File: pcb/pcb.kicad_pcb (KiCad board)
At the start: 2 copper layers, 30 parts, among them J1 USB_C_Receptacle_PowerOnly_6P, J10 Screw_Terminal_01x03, J2 Conn_01x04_Pin, J3 Screw_Terminal_01x03, J4 Screw_Terminal_01x04, J5 Screw_Terminal_01x02, J6 Screw_Terminal_01x02, J7 Screw_Terminal_01x04, J8 Screw_Terminal_01x07, J9 Screw_Terminal_01x02, K1 SANYOU_SRD_Form_A, Q1 2N2222A, Q2 AO3400A, U1 AMS1117-3.3, U2 ESP32-C6-MINI-1, U3 AM2302

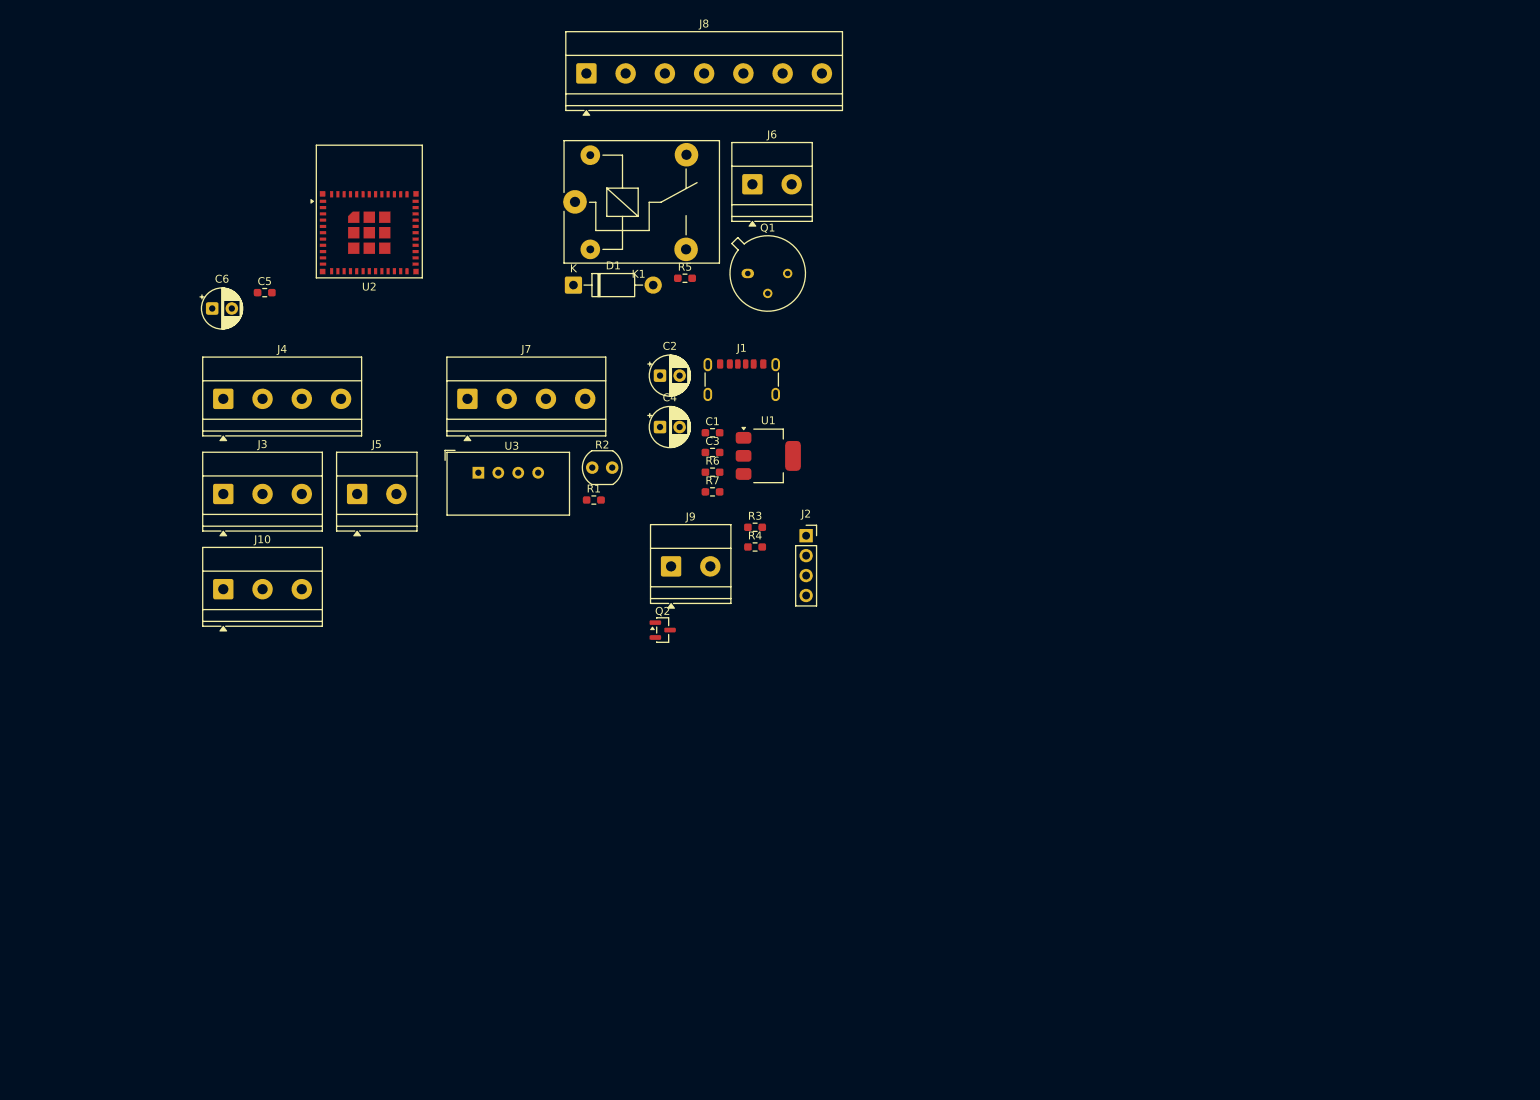
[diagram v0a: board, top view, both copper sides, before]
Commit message: placing the components
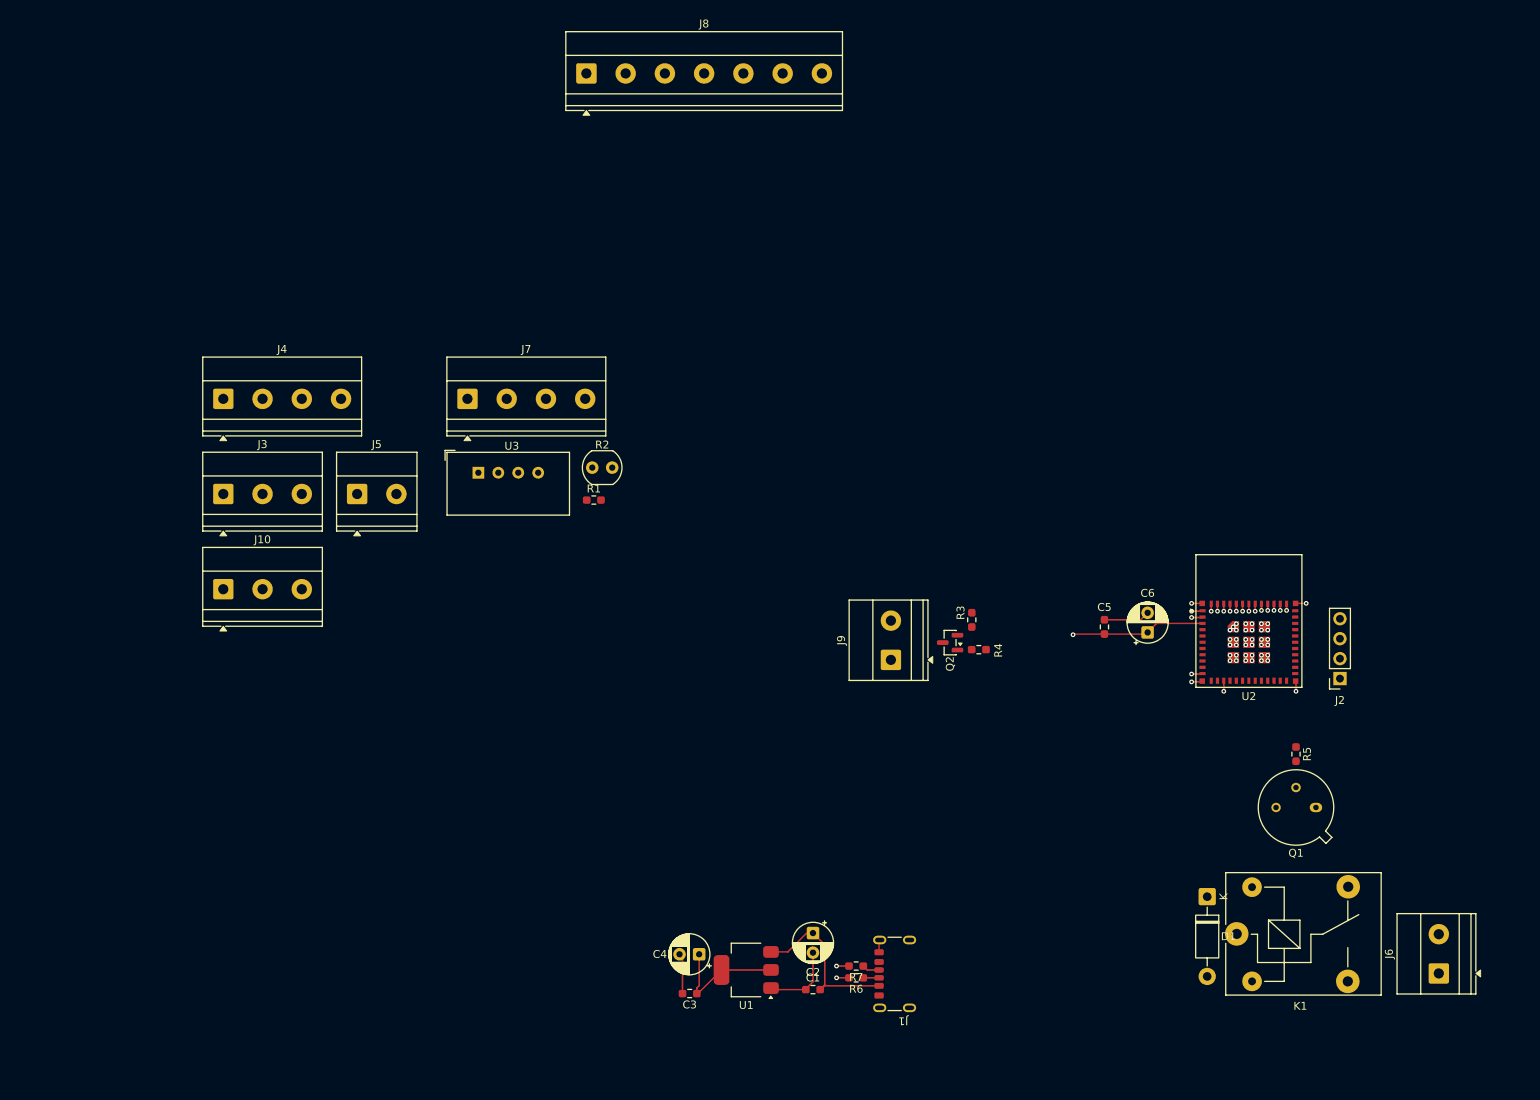
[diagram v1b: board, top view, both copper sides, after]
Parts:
- moved J6 133.2 mm to (244.1, 140.1), turned to 90 degrees
- moved C6 126.1 mm to (207.0, 96.7), turned to 90 degrees
- moved K1 125.7 mm to (218.3, 135.1)
- moved U2 123.6 mm to (219.9, 98.0)
- moved C5 115.1 mm to (201.5, 96.0), turned to 90 degrees
- moved D1 112.2 mm to (214.6, 130.4), turned to -90 degrees
- moved Q1 99.3 mm to (228.4, 119.0), turned to 180 degrees
- moved R5 98.6 mm to (225.9, 112.2), turned to -90 degrees
- moved J1 77.4 mm to (175.9, 140.2), turned to 90 degrees
- moved C2 73.6 mm to (164.4, 135.0), turned to -90 degrees
- moved C1 72.1 mm to (164.4, 142.2), turned to 180 degrees
- moved J2 70.4 mm to (231.5, 102.6), turned to 180 degrees
- moved C3 69.0 mm to (148.7, 142.7), turned to 180 degrees
- moved C4 67.3 mm to (149.9, 137.7), turned to 180 degrees
- moved R6 67.0 mm to (169.9, 140.7), turned to 180 degrees
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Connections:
- Q1 pad 1: unconnected-(Q1-E-Pad1) -> GND
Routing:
- net GND: track 0.00 -> 48.7 mm, vias 0 -> 59
- net +3.3V: track 0.00 -> 32.9 mm, vias 0 -> 1
- net +5V: track 0.00 -> 22.1 mm
- net Net-(J1-CC2): track 0.00 -> 2.21 mm
- net Net-(J1-CC1): track 0.00 -> 2.01 mm
- net Net-(J6-Pin_1): track 0.00 -> 1.43 mm
- added copper zone on In2.Cu, net +3.3V
- added copper zone on In1.Cu, net GND
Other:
- copper layers 2 -> 4

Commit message: aligning components and routing
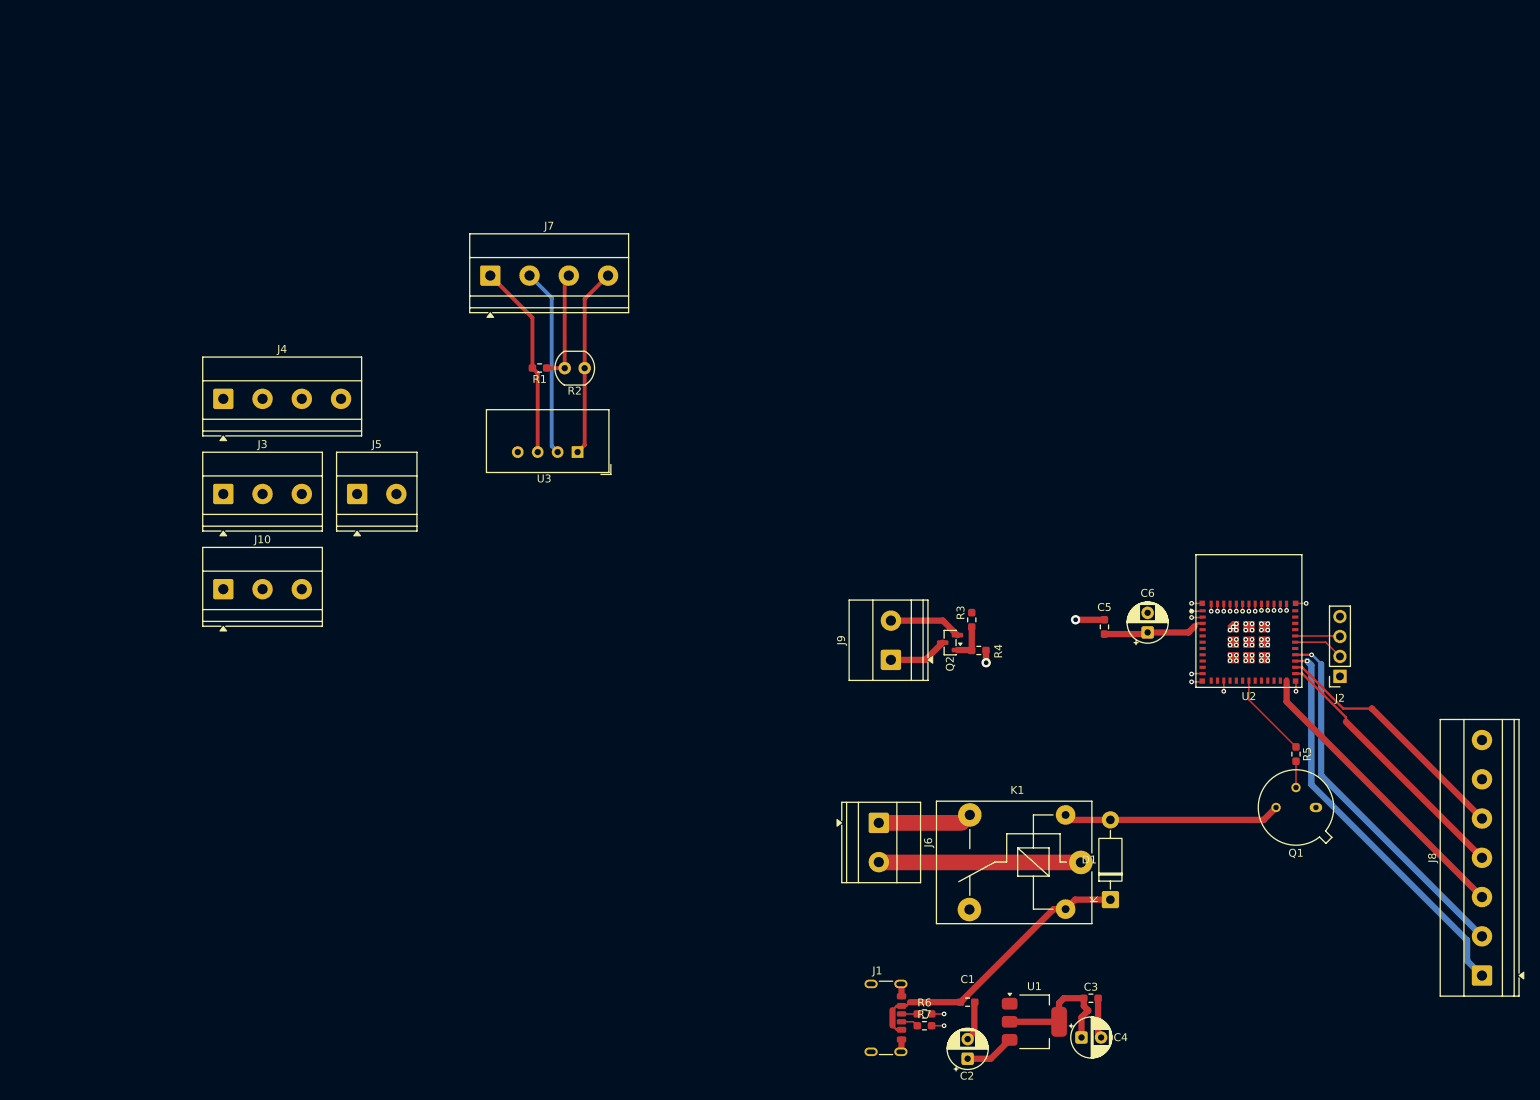
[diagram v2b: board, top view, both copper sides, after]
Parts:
- moved J8 161.9 mm to (249.6, 140.4), turned to 90 degrees
- moved J6 73.9 mm to (172.8, 121.0), turned to -90 degrees
- moved C3 51.1 mm to (199.8, 143.3), turned to 0 degrees
- moved C4 49.8 mm to (198.6, 148.3), turned to 0 degrees
- moved U1 37.3 mm to (192.6, 146.3), turned to 0 degrees
- moved C2 25.4 mm to (184.1, 151.0), turned to 90 degrees
- moved K1 21.8 mm to (198.5, 126.0), turned to 180 degrees
- moved C1 19.8 mm to (184.1, 143.8), turned to 0 degrees
- moved R1 18.2 mm to (129.6, 63.0), turned to 180 degrees
- moved J7 16.0 mm to (123.3, 51.2)
- moved U3 12.9 mm to (134.4, 73.7), turned to 180 degrees
- moved R2 12.7 mm to (135.3, 63.0), turned to 180 degrees
- moved D1 12.3 mm to (202.3, 130.7), turned to 90 degrees
- moved R7 11.6 mm to (178.6, 146.8), turned to 0 degrees
- moved R6 9.84 mm to (178.6, 145.3), turned to 0 degrees
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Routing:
- net /screen/rst: track 0.00 -> 50.8 mm, vias 0 -> 1
- net /screen/cs: track 0.00 -> 49.3 mm, vias 0 -> 1
- net /screen/dc: track 0.00 -> 37.9 mm
- net /screen/sda: track 0.00 -> 33.8 mm
- net /screen/scl: track 0.00 -> 31.8 mm
- net Net-(D1-A): track 0.00 -> 27.7 mm
- net Net-(J6-Pin_2): track 0.20 -> 26.0 mm
- net GND1: track 0.00 -> 25.0 mm
- net VDD: track 0.00 -> 24.1 mm
- net Net-(J7-Pin_2): track 0.00 -> 24.0 mm
- net +5V: track 22.1 -> 43.3 mm
- net Net-(J7-Pin_3): track 0.00 -> 14.3 mm
- net Net-(J6-Pin_1): track 1.43 -> 13.4 mm
- net /Pump control/PUMP_control: track 0.00 -> 10.9 mm
- net Net-(J9-Pin_1): track 0.00 -> 7.51 mm
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
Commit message: finishing the pathing
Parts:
- moved C3 111.3 mm to (107.0, 81.8), turned to 90 degrees
- moved J2 108.6 mm to (129.0, 66.2)
- moved J8 108.6 mm to (147.1, 104.3)
- moved R5 108.6 mm to (123.4, 76.1)
- moved U2 108.6 mm to (117.4, 61.8)
- moved C5 108.6 mm to (99.0, 59.9)
- moved C6 108.6 mm to (104.5, 60.6)
- moved D1 108.6 mm to (99.8, 94.6)
- moved J6 108.6 mm to (70.3, 84.8)
- moved K1 108.6 mm to (96.0, 89.9)
- moved Q1 108.6 mm to (126.0, 82.9)
- moved C4 108.4 mm to (112.0, 83.0), turned to 90 degrees
- moved J9 105.7 mm to (70.9, 78.2)
- moved Q2 105.7 mm to (78.5, 76.0)
- moved R3 105.7 mm to (81.2, 73.1)
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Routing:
- net /led_control/LED_control: track 0.00 -> 55.9 mm
- net /Sensor inputs/soil_temp: track 0.00 -> 49.2 mm
- net /Sensor inputs/water level: track 0.00 -> 46.8 mm
- net /Sensor inputs/light sensor: track 0.00 -> 45.1 mm, vias 0 -> 1
- net /Sensor inputs/air sensor: track 0.00 -> 35.4 mm, vias 0 -> 1
- net /Sensor inputs/humidity: track 0.00 -> 33.3 mm
- net Net-(D1-A): track 27.7 -> 32.3 mm
- net GND: track 54.8 -> 51.6 mm
- net +5V: track 43.3 -> 42.6 mm
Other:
- board outline added: 94.5 x 99.4 mm

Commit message: realigning the pcb
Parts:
- added REF**: MountingHole_3.2mm_M3, MountingHole:MountingHole_3.2mm_M3, F.Cu at (68.9, 125.1)
- added REF**: MountingHole_3.2mm_M3, MountingHole:MountingHole_3.2mm_M3, F.Cu at (147.8, 66.8)
- U2: footprint RF_Module:ESP32-C6-MINI-1 -> Library:ESP32-C6-MINI-1psa
- moved R2 70.8 mm to (82.0, 47.2)
- moved J7 70.8 mm to (70.2, 59.2)
- moved R1 70.8 mm to (82.0, 52.9)
- moved U3 70.8 mm to (92.7, 48.1)
- moved C6 20.5 mm to (105.1, 81.0)
- moved J5 20.5 mm to (71.4, 70.8)
- moved C1 20.5 mm to (108.1, 117.9)
- moved C2 20.5 mm to (115.3, 117.9)
- moved C3 20.5 mm to (107.6, 102.2)
- moved C4 20.5 mm to (112.6, 103.4)
- moved D1 20.5 mm to (100.4, 115.1)
- moved J1 20.5 mm to (103.6, 127.0)
- moved J10 20.5 mm to (71.4, 87.2)
- moved J2 20.5 mm to (129.6, 86.6)
- moved J3 20.5 mm to (81.8, 68.2)
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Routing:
- net GND1: track 25.0 -> 27.5 mm
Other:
- board size 94.5 x 99.4 mm -> 88.3 x 88.2 mm
- board text added: "V cut"

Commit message: finishing the pcb
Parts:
- added REF**: MountingHole_2.2mm_M2, MountingHole:MountingHole_2.2mm_M2, F.Cu at (85.8, 43.6)
- added REF**: MountingHole_2.2mm_M2, MountingHole:MountingHole_2.2mm_M2, F.Cu at (79.6, 59.6)
- moved U3 2.05 mm to (93.4, 50.0)
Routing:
- net Net-(J7-Pin_2): track 24.0 -> 1.91 mm
- net GND1: track 27.5 -> 14.0 mm
- net VDD: track 24.1 -> 13.0 mm

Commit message: adding text to the pcb
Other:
- board text added: "Designed in Budapest"
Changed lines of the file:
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@@
 			(at 0 -4.15 0)
 			(layer "F.SilkS")
+			(hide yes)
 			(effects
 				(font
@@
 			(at 0 -4.15 0)
 			(layer "F.SilkS")
+			(hide yes)
 			(effects
 				(font
@@
 		(layer "Edge.Cuts")
 	)
+	(gr_text "Designed in Budapest"
+		(at 86.2 94.6 0)
+		(layer "F.SilkS")
+		(effects
+			(font
+				(size 2 2)
+				(thickness 0.25)
+			)
+			(justify left bottom)
+		)
+	)
 	(gr_text "V cut"

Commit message: polishing the pcb
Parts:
- removed the REF** at (85.8, 43.6)
- removed the REF** at (79.6, 59.6)
- U3: footprint Sensor:ASAIR_AM2302_P2.54mm_Vertical -> Sensor:ASAIR_AM2302_P2.54mm_Lead2.75mm_TabDown
- moved U3 4.98 mm to (89.2, 47.3), turned to 0 degrees
- moved R1 3.06 mm to (83.0, 55.8)
- moved R2 1.46 mm to (83.0, 46.1)
- moved J7 0.10 mm to (70.2, 59.1)
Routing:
- net VDD: track 13.0 -> 34.0 mm
- net Net-(J7-Pin_2): track 1.91 -> 20.8 mm
- net GND1: track 14.0 -> 26.7 mm
- net Net-(J7-Pin_3): track 14.3 -> 19.2 mm
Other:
- board size 88.3 x 88.2 mm -> 88.3 x 102.2 mm

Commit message: trieing to make a 3d model from the shematic and fixing some issues about the esp32 gipos
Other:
- board size 88.3 x 102.2 mm -> 88.3 x 88.4 mm
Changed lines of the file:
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@@
 		(allow_soldermask_bridges_in_footprints no)
 		(tenting front back)
-		(grid_origin 64.6 111)
+		(grid_origin 152.739432 62.2)
 		(pcbplotparams
 			(layerselection 0x00000000_00000000_55555555_5755f5ff)
@@
 	)
 	(gr_line
-		(start 152.9 62.2)
+		(start 120.2 62.2)
+		(end 120.2 41)
+		(stroke
+			(width 0.1)
+			(type default)
+		)
+		(layer "Dwgs.User")
+	)
+	(gr_line
+		(start 152.839432 62.2)
 		(end 64.4 62.2)
 		(stroke
@@
 	)
 	(gr_rect
-		(start 64.47 27.2)
+		(start 64.47 41)
 		(end 152.739432 129.4)
 		(stroke
@@
 			)
 			(justify left bottom)
+		)
+	)
+	(gr_text "V cut"
+		(at 120.2 52 0)
+		(layer "Cmts.User")
+		(effects
+			(font
+				(size 1 1)
+				(thickness 0.15)
+			)
+			(justify left bottom)
